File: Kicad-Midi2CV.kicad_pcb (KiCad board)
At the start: 2 copper layers, 99.1 x 99.1 mm, 63 parts, among them IC1 MCP4725module, IC2 MCP4725module, J1 Barrel_Jack, J10 AudioJack2_Ground_Switch, J11 AudioJack2_Ground_Switch, J12 AudioJack2_Ground_Switch, J13 AudioJack2_Ground_Switch, J2 DIN-5, J3 AudioJack2_Ground_Switch, J4 Conn_01x04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

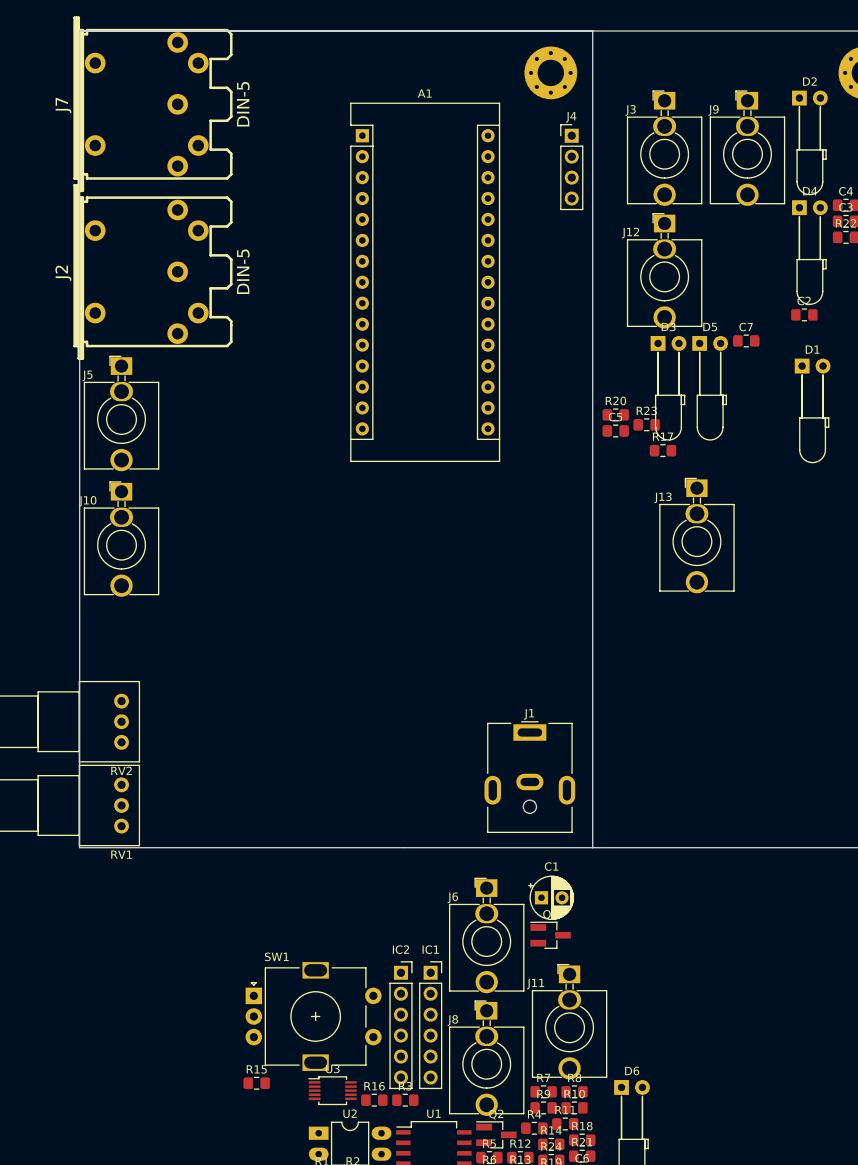
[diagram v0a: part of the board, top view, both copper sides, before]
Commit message: Jack I/O
Label jacks
Voltage div on CV in / A3
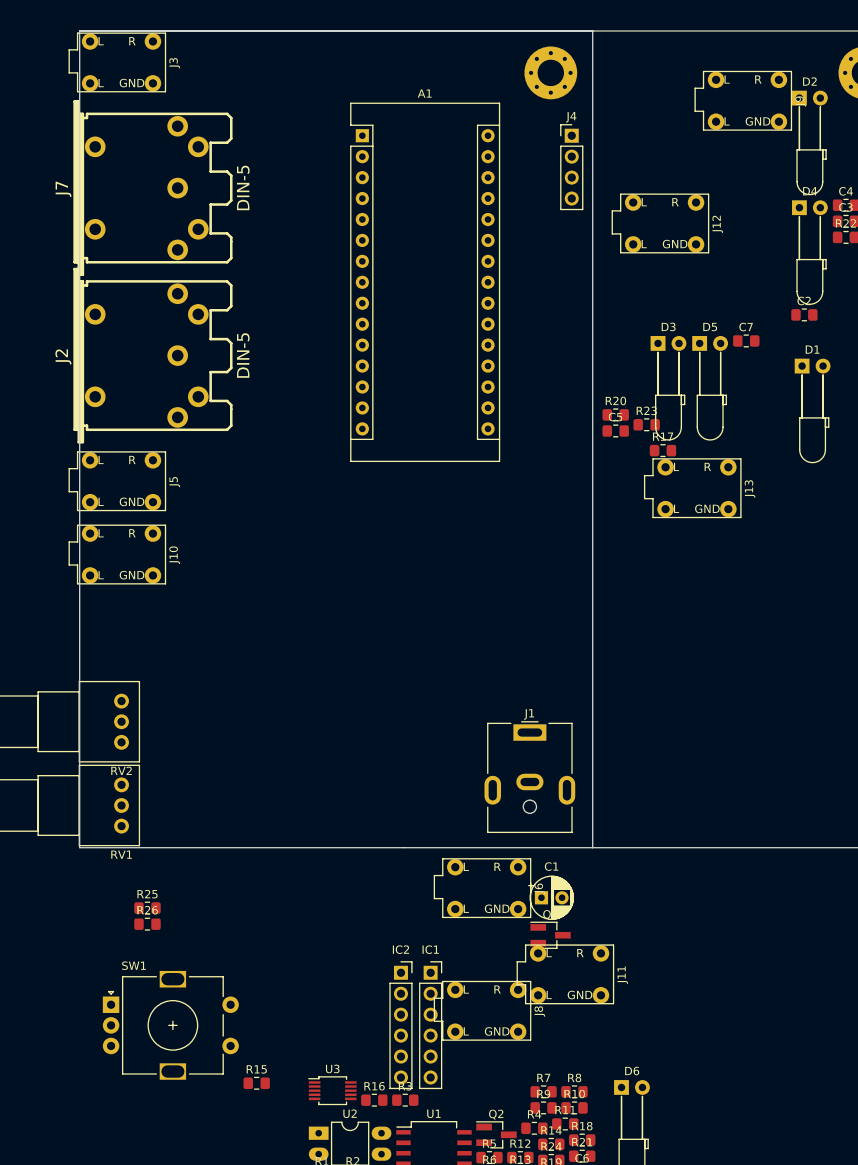
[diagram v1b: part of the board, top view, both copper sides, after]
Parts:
- added R25: 10k, Resistor_SMD:R_0805_2012Metric_Pad1.15x1.40mm_HandSolder, F.Cu at (33.6, 131.8)
- added R26: 10k, Resistor_SMD:R_0805_2012Metric_Pad1.15x1.40mm_HandSolder, F.Cu at (33.6, 133.7)
- J10: value AudioJack2_Ground_Switch -> Gate1; footprint Connector_Audio:Jack_3.5mm_QingPu_WQP-PJ398SM_Vertical_CircularHoles -> Connector_Audio:AudioJack3StereoNarrow-PJ-321
- J11: value AudioJack2_Ground_Switch -> Gate2; footprint Connector_Audio:Jack_3.5mm_QingPu_WQP-PJ398SM_Vertical_CircularHoles -> Connector_Audio:AudioJack3StereoNarrow-PJ-321
- J12: value AudioJack2_Ground_Switch -> Gate3; footprint Connector_Audio:Jack_3.5mm_QingPu_WQP-PJ398SM_Vertical_CircularHoles -> Connector_Audio:AudioJack3StereoNarrow-PJ-321
- J13: value AudioJack2_Ground_Switch -> Gate4; footprint Connector_Audio:Jack_3.5mm_QingPu_WQP-PJ398SM_Vertical_CircularHoles -> Connector_Audio:AudioJack3StereoNarrow-PJ-321
- J3: value AudioJack2_Ground_Switch -> CV in; footprint Connector_Audio:Jack_3.5mm_QingPu_WQP-PJ398SM_Vertical_CircularHoles -> Connector_Audio:AudioJack3StereoNarrow-PJ-321
- J5: value AudioJack2_Ground_Switch -> CV1; footprint Connector_Audio:Jack_3.5mm_QingPu_WQP-PJ398SM_Vertical_CircularHoles -> Connector_Audio:AudioJack3StereoNarrow-PJ-321
- J6: value AudioJack2_Ground_Switch -> CV2; footprint Connector_Audio:Jack_3.5mm_QingPu_WQP-PJ398SM_Vertical_CircularHoles -> Connector_Audio:AudioJack3StereoNarrow-PJ-321
- J8: value AudioJack2_Ground_Switch -> CV3; footprint Connector_Audio:Jack_3.5mm_QingPu_WQP-PJ398SM_Vertical_CircularHoles -> Connector_Audio:AudioJack3StereoNarrow-PJ-321
- J9: value AudioJack2_Ground_Switch -> CV4; footprint Connector_Audio:Jack_3.5mm_QingPu_WQP-PJ398SM_Vertical_CircularHoles -> Connector_Audio:AudioJack3StereoNarrow-PJ-321
- R10: value 8k2 -> 10k
- R11: value 1k -> 8k2
- R12: value 220R -> 8k2
- R14: value 0R -> 220R
- R15: value 0R -> 1k
- R16, R17: value 680R -> 0R
- R22, R23: value 10k -> 680R
- R8: value 1k -> 10k
- R9: value 8k2 -> 1k
- moved J3 66.0 mm to (30.5, 29.2)
- moved SW1 17.3 mm to (29.2, 143.5)
- moved J5 14.0 mm to (30.5, 80.0)
- moved J7 10.2 mm to (34.3, 44.5)
- moved J2 10.2 mm to (34.3, 64.8)
- moved J10 7.62 mm to (30.5, 88.9)
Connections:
- J3 pad T: A3 -> Net-(J3-PadT)
- R10 pad 1: /SCL -> GND
- R10 pad 2: +5V -> A3
- R11 pad 1: /RX -> /SDA
- R12 pad 1: Net-(R12-Pad1) -> /SCL
- R12 pad 2: Net-(J7-Pad4) -> +5V
- R13 pad 1: GND -> /RX
- R13 pad 2: /MIDI-IN -> +5V
- R14 pad 1: CV2 -> Net-(R14-Pad1)
- R14 pad 2: Net-(IC1-Pad1) -> Net-(J7-Pad4)
- R15 pad 1: CV1 -> GND
- R15 pad 2: Net-(IC2-Pad1) -> /MIDI-IN
- R16 pad 1: LED1 -> CV2
- R16 pad 2: Net-(D1-Pad2) -> Net-(IC1-Pad1)
- R17 pad 1: LED2 -> CV1
- R17 pad 2: Net-(D2-Pad2) -> Net-(IC2-Pad1)
- R18 pad 1: LED3 -> LED1
- R18 pad 2: Net-(D3-Pad2) -> Net-(D1-Pad2)
- R19 pad 1: LED4 -> LED2
- R19 pad 2: Net-(D4-Pad2) -> Net-(D2-Pad2)
- R20 pad 1: LED-sel -> LED3
- R20 pad 2: Net-(D5-Pad2) -> Net-(D3-Pad2)
- R21 pad 1: LED-sel2 -> LED4
- R21 pad 2: Net-(D6-Pad2) -> Net-(D4-Pad2)
- R22 pad 1: Net-(R22-Pad1) -> LED-sel
- R22 pad 2: Btn -> Net-(D5-Pad2)
- R23 pad 1: Net-(C6-Pad1) -> LED-sel2
- R23 pad 2: A2 -> Net-(D6-Pad2)
- R24 pad 1: Net-(C7-Pad1) -> Net-(R24-Pad1)
- R24 pad 2: A1 -> Btn
- R8 pad 1: GND -> Net-(J3-PadT)
- R8 pad 2: /TX -> A3
- R9 pad 1: /SDA -> GND
- R9 pad 2: +5V -> /TX
- SW1 pad S2: Net-(R22-Pad1) -> Net-(R24-Pad1)
- U2 pad 1: Net-(R12-Pad1) -> Net-(R14-Pad1)

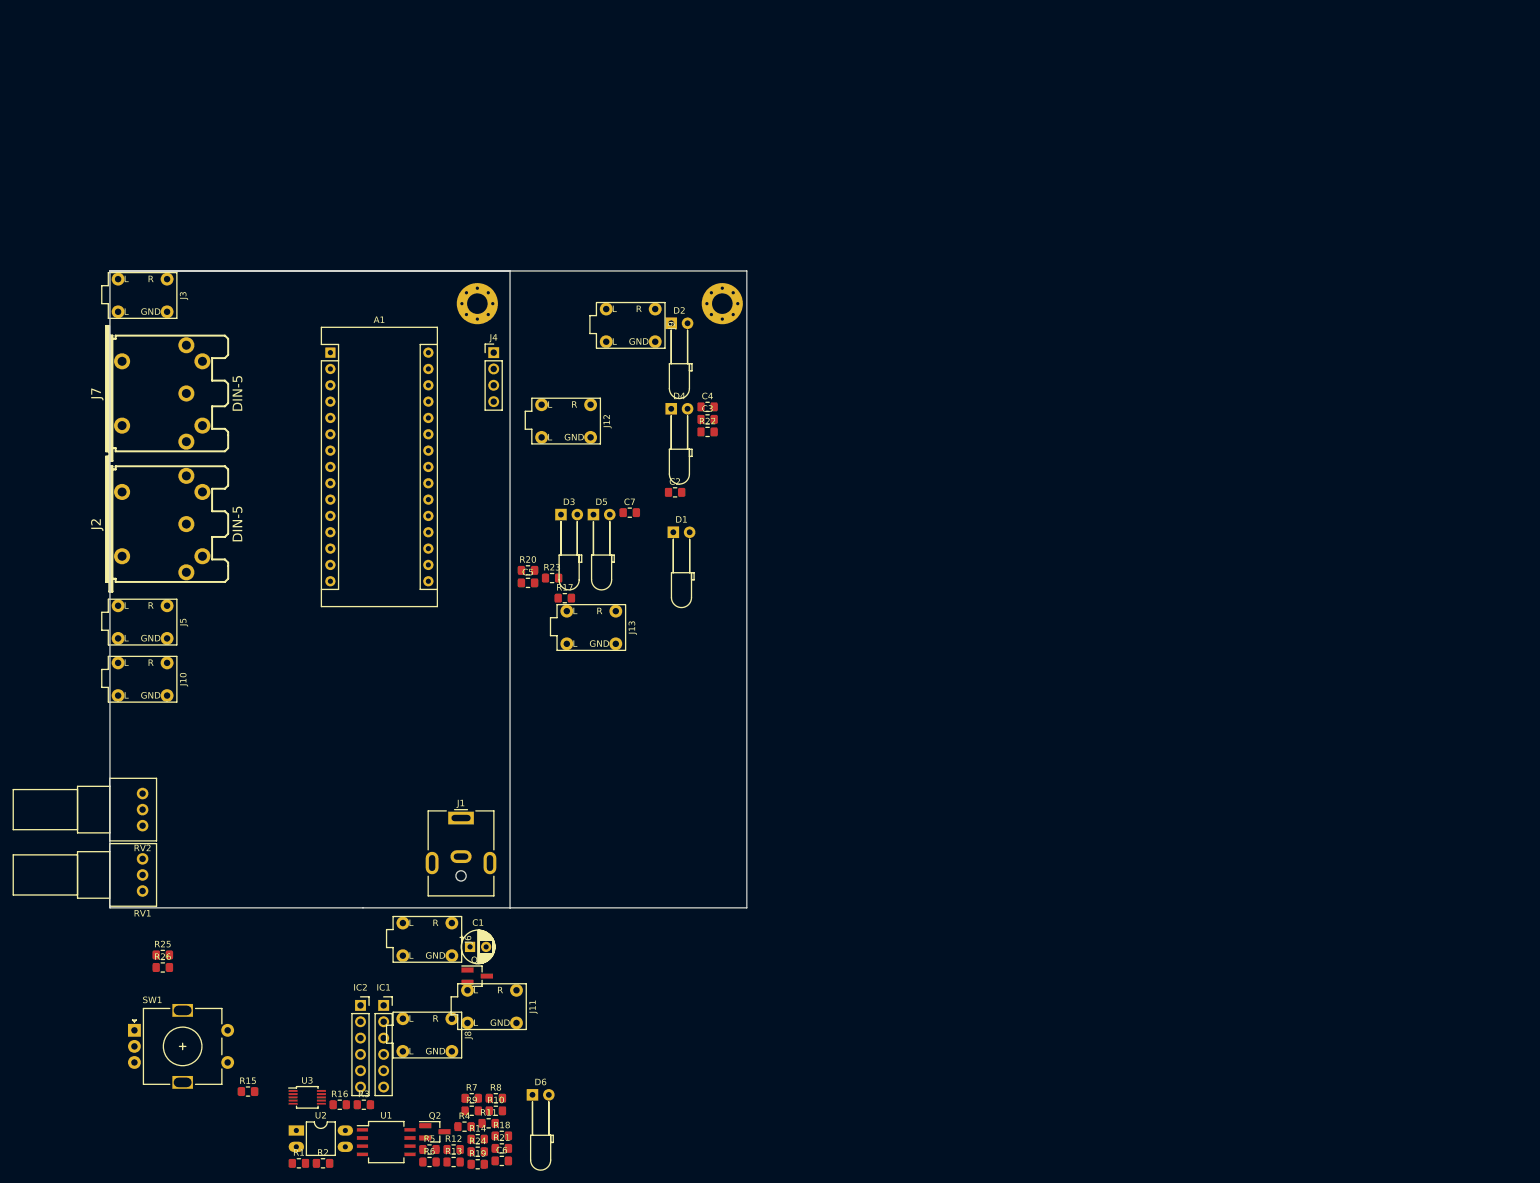
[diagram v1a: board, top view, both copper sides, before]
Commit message: Names to remaining IO
MIDI
LED
Pots are kept as RV1 and RV2 as it matches CV1 and CV2
Front panel rearranged
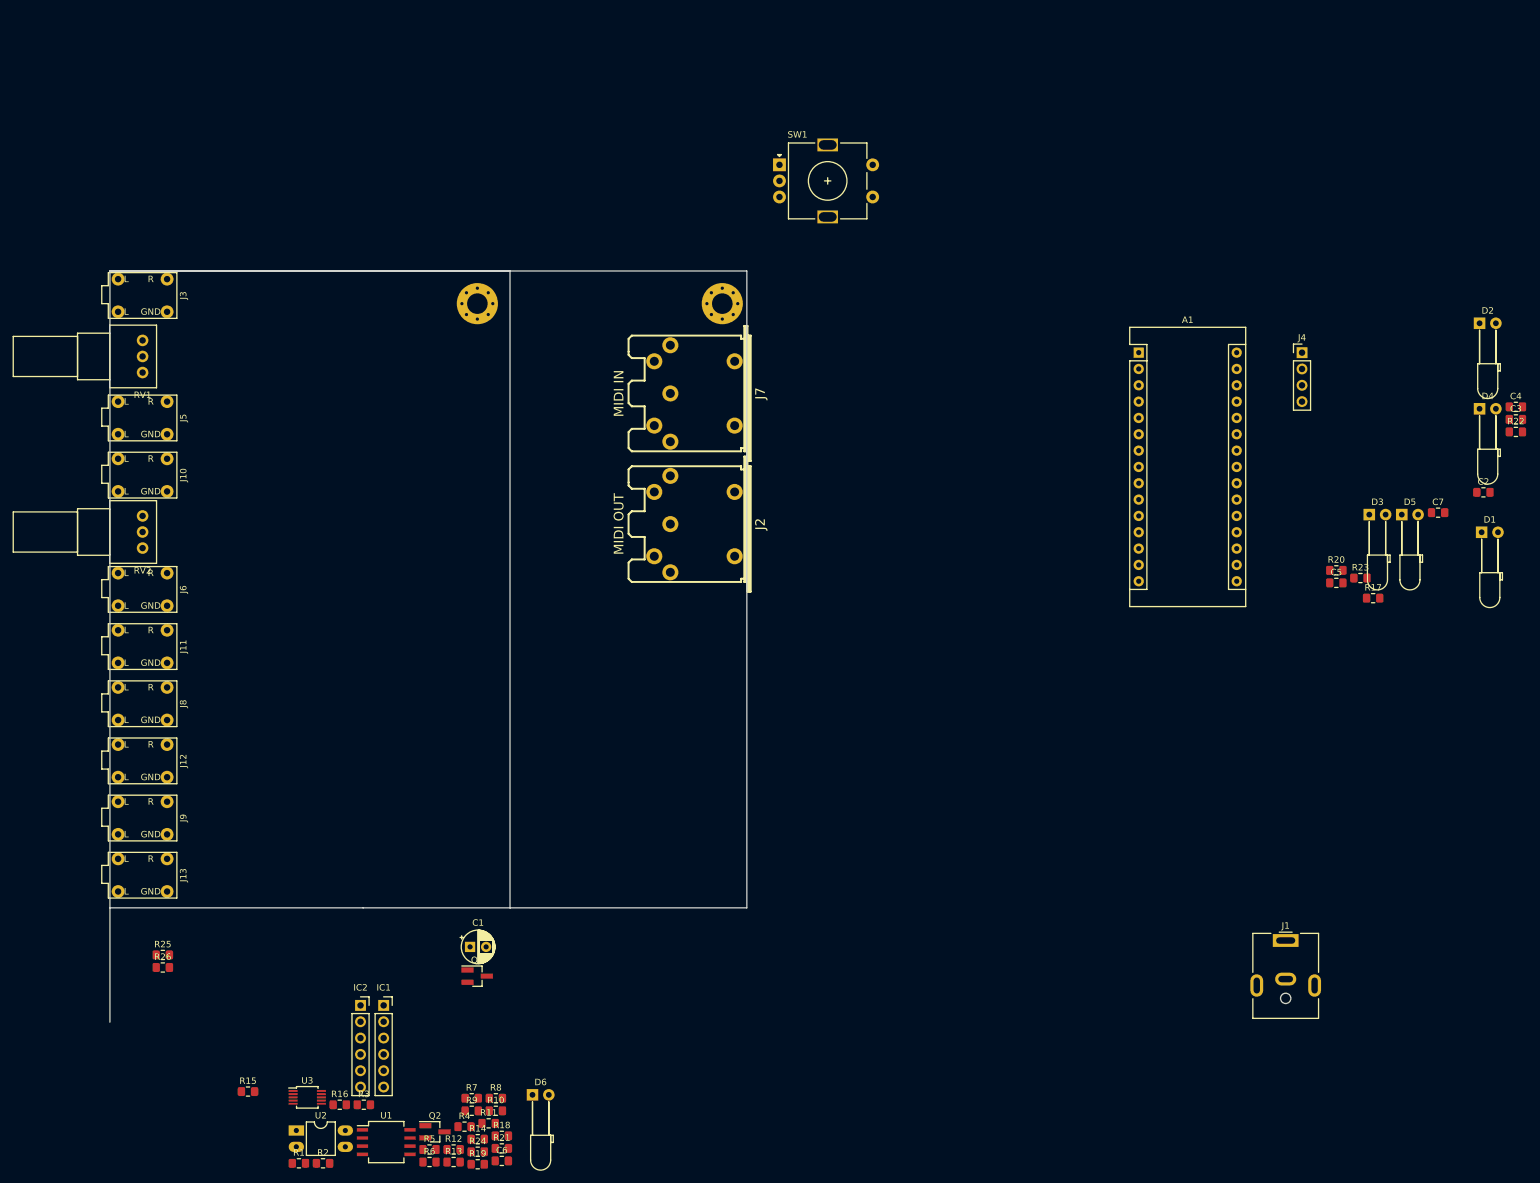
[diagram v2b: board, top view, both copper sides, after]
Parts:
- D1: value LED -> LED1
- D2: value LED -> LED2
- D3: value LED -> LED3
- D4: value LED -> LED4
- D5: value LED -> LEDset1
- D6: value LED -> LEDset2
- J1: value Barrel_Jack -> Vin 7-12v
- J2: value DIN-5 -> MIDI OUT
- J7: value DIN-5 -> MIDI IN
- SW1: value Rotary_Encoder_Switch -> Encoder_Selector
- moved SW1 167.9 mm to (129.5, 8.89)
- moved J1 129.7 mm to (208.3, 129.5)
- moved C7 125.7 mm to (232.0, 63.0)
- moved C3 125.7 mm to (244.1, 48.5)
- moved C4 125.7 mm to (244.1, 46.5)
- moved C5 125.7 mm to (216.2, 73.9)
- moved D2 125.7 mm to (238.4, 33.5)
- moved D4 125.7 mm to (238.4, 46.8)
- moved D5 125.7 mm to (226.3, 63.3)
- moved R20 125.7 mm to (216.2, 72.0)
- moved R22 125.7 mm to (244.1, 50.4)
- moved R23 125.7 mm to (219.9, 73.2)
- moved A1 125.7 mm to (185.4, 38.1)
- moved C2 125.7 mm to (239.0, 59.8)
- moved D1 125.7 mm to (238.8, 66.0)
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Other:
- board size 99.1 x 99.1 mm -> 99.1 x 116.8 mm

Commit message: PCB misc
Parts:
- moved J11 0.64 mm to (30.5, 84.5)
- moved J12 0.64 mm to (30.5, 102.2)
- moved J13 0.64 mm to (30.5, 120.0)
- moved J8 0.64 mm to (30.5, 93.3)
- moved J9 0.64 mm to (30.5, 111.1)
- moved RV2 0.64 mm to (30.5, 64.1)
- moved J6 0.63 mm to (30.5, 75.6)
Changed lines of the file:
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@@
   )
   (module Potentiometer_THT:Potentiometer_Alps_RK097_Single_Horizontal (layer F.Cu)
-    (at 30.48 63.5 180)
+    (at 30.48 64.135 180)
     (descr "Potentiometer, horizontal, Alps RK097 Single, http://www.alps.com/prod/info/E/HTML/Potentiometer/RotaryPotentiometers/RK097/RK097_list.html")
     (tags "Potentiometer horizontal Alps RK097 Single")
@@
   )
   (module Connector_Audio:AudioJack3StereoNarrow-PJ-321 (layer F.Cu)
-    (at 30.48 74.93)
+    (at 30.48 75.565)
     (fp_text reference J6 (at 6.35 0 90) (layer F.SilkS)
       (effects (font (size 1 1) (thickness 0.15)))
@@
   )
   (module Connector_Audio:AudioJack3StereoNarrow-PJ-321 (layer F.Cu)
-    (at 30.48 92.71)
+    (at 30.48 93.345)
     (fp_text reference J8 (at 6.35 0 90) (layer F.SilkS)
       (effects (font (size 1 1) (thickness 0.15)))
@@
   )
   (module Connector_Audio:AudioJack3StereoNarrow-PJ-321 (layer F.Cu)
-    (at 30.48 110.49)
+    (at 30.48 111.125)
     (fp_text reference J9 (at 6.35 0 90) (layer F.SilkS)
       (effects (font (size 1 1) (thickness 0.15)))
@@
   )
   (module Connector_Audio:AudioJack3StereoNarrow-PJ-321 (layer F.Cu)
-    (at 30.48 83.82)
+    (at 30.48 84.455)
     (fp_text reference J11 (at 6.35 0 90) (layer F.SilkS)
       (effects (font (size 1 1) (thickness 0.15)))
@@
   )
   (module Connector_Audio:AudioJack3StereoNarrow-PJ-321 (layer F.Cu)
-    (at 30.48 101.6)
+    (at 30.48 102.235)
     (fp_text reference J12 (at 6.35 0 90) (layer F.SilkS)
       (effects (font (size 1 1) (thickness 0.15)))
@@
   )
   (module Connector_Audio:AudioJack3StereoNarrow-PJ-321 (layer F.Cu)
-    (at 30.48 119.38)
+    (at 30.48 120.015)
     (fp_text reference J13 (at 6.35 0 90) (layer F.SilkS)
       (effects (font (size 1 1) (thickness 0.15)))

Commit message: PCB
Misc - minor
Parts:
- added NA: Mounting3.2mm, MountingHole:MountingHole_3.2mm_M3_Pad_Via, F.Cu at (50.8, 120.7)
- added NA: Mounting3.2mm, MountingHole:MountingHole_3.2mm_M3_Pad_Via, F.Cu at (50.8, 89.5)
- moved D2 127.4 mm to (121.9, 85.1), turned to 90 degrees
- moved D4 126.4 mm to (121.9, 95.9), turned to 90 degrees
- moved D1 117.6 mm to (121.9, 79.4), turned to 90 degrees
- moved D5 113.1 mm to (121.9, 106.7), turned to 90 degrees
- moved A1 104.7 mm to (85.1, 67.9), turned to 180 degrees
- moved D3 102.9 mm to (121.9, 90.2), turned to 90 degrees
- moved SW1 100.0 mm to (92.1, 101.6)
- moved D6 60.4 mm to (121.9, 101.6), turned to 90 degrees
- moved NA 31.9 mm to (50.7, 30.5)
- moved NA 21.0 mm to (99.7, 29.8)
- moved J7 8.26 mm to (115.6, 36.2)
- moved J2 8.25 mm to (115.6, 56.5)
- moved J11 0.90 mm to (31.1, 85.1)
- moved J12 0.90 mm to (31.1, 102.9)
- moved J13 0.90 mm to (31.1, 120.7)
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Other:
- board size 99.1 x 116.8 mm -> 99.7 x 99.7 mm
- board text added: "(125.1,25.4)"
- board text added: "(25.4,25,4)"
